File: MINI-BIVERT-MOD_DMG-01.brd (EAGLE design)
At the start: 15.6 x 10.5 mm, 2 parts

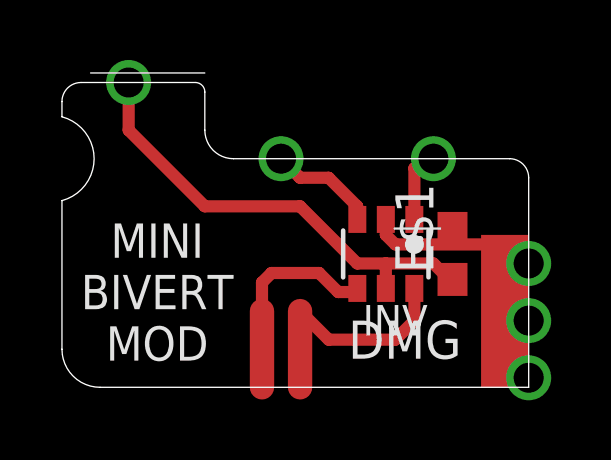
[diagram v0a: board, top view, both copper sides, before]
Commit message: Silkscreen minor updates
Removed component names and values on silkscreen.
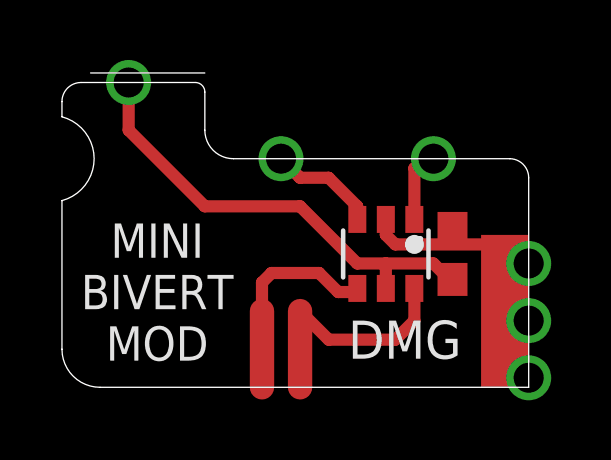
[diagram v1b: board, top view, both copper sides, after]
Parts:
- C: value (none) -> 100nF
- INV: value (none) -> SN74LVC2G04
- renumbered E$1 to C
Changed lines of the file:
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@@
 <layer number="23" name="tOrigins" color="15" fill="1" visible="yes" active="yes"/>
 <layer number="24" name="bOrigins" color="15" fill="1" visible="yes" active="yes"/>
-<layer number="25" name="tNames" color="7" fill="1" visible="no" active="yes"/>
-<layer number="26" name="bNames" color="7" fill="1" visible="no" active="yes"/>
-<layer number="27" name="tValues" color="7" fill="1" visible="no" active="yes"/>
-<layer number="28" name="bValues" color="7" fill="1" visible="no" active="yes"/>
+<layer number="25" name="tNames" color="7" fill="1" visible="yes" active="yes"/>
+<layer number="26" name="bNames" color="7" fill="1" visible="yes" active="yes"/>
+<layer number="27" name="tValues" color="7" fill="1" visible="yes" active="yes"/>
+<layer number="28" name="bValues" color="7" fill="1" visible="yes" active="yes"/>
 <layer number="29" name="tStop" color="7" fill="3" visible="yes" active="yes"/>
 <layer number="30" name="bStop" color="7" fill="6" visible="yes" active="yes"/>
@@
 </autorouter>
 <elements>
-<element name="INV" library="linear" library_urn="urn:adsk.eagle:library:262" package="SOT23-6" package3d_urn="urn:adsk.eagle:package:16490/2" value="" x="10.795" y="4.445" rot="R180"/>
-<element name="E$1" library="rcl" library_urn="urn:adsk.eagle:library:334" package="C0603" package3d_urn="urn:adsk.eagle:package:23616/2" value="" x="13.0175" y="4.445" rot="R90"/>
+<element name="INV" library="linear" library_urn="urn:adsk.eagle:library:262" package="SOT23-6" package3d_urn="urn:adsk.eagle:package:16490/2" value="SN74LVC2G04" x="10.795" y="4.445" smashed="yes" rot="R180"/>
+<element name="C" library="rcl" library_urn="urn:adsk.eagle:library:334" package="C0603" package3d_urn="urn:adsk.eagle:package:23616/2" value="100nF" x="13.0175" y="4.445" smashed="yes" rot="R90"/>
 </elements>
 <signals>
